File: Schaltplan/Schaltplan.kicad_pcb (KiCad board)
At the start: 2 copper layers, 12 parts, among them IC1 STM32G031J6M6, J1 Conn_01x01, J2 Conn_02x03_Odd_Even, SW1 SW_SPDT, U1 HU2032-LF

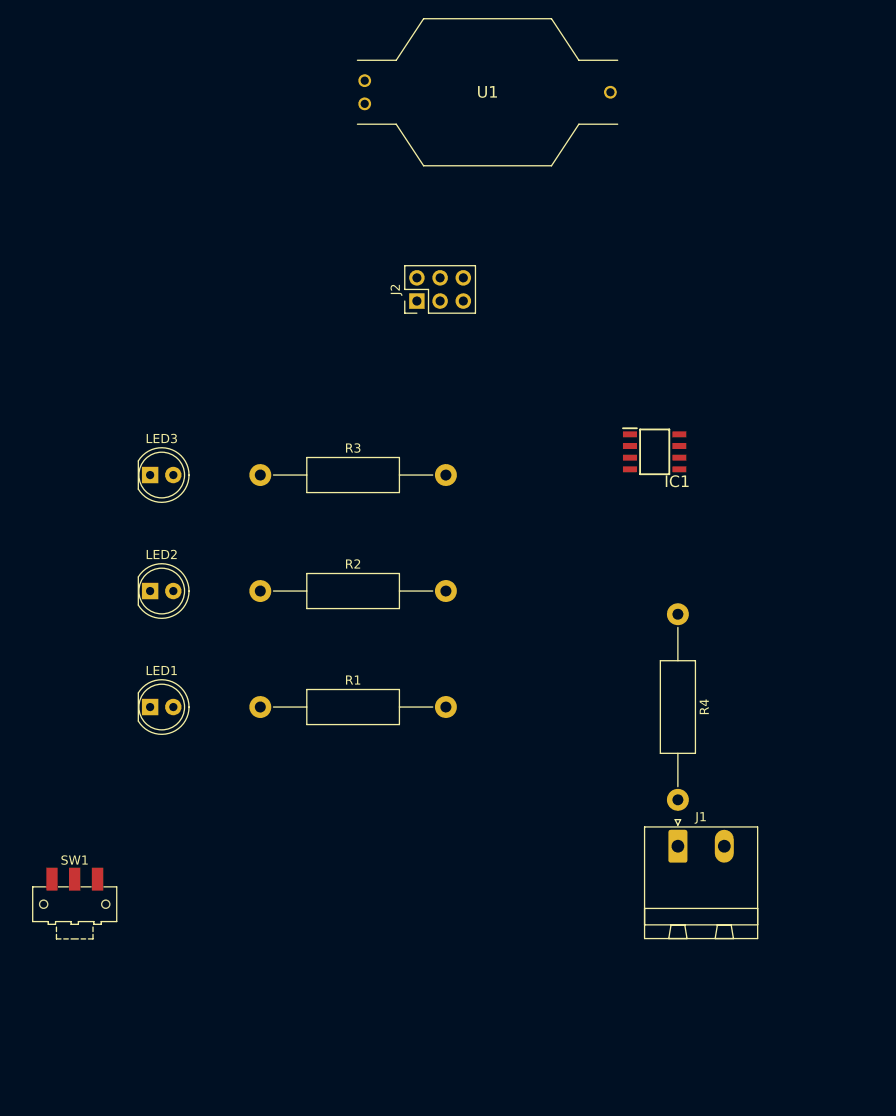
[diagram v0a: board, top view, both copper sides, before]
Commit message: ersten Leiterbahnen gezogen
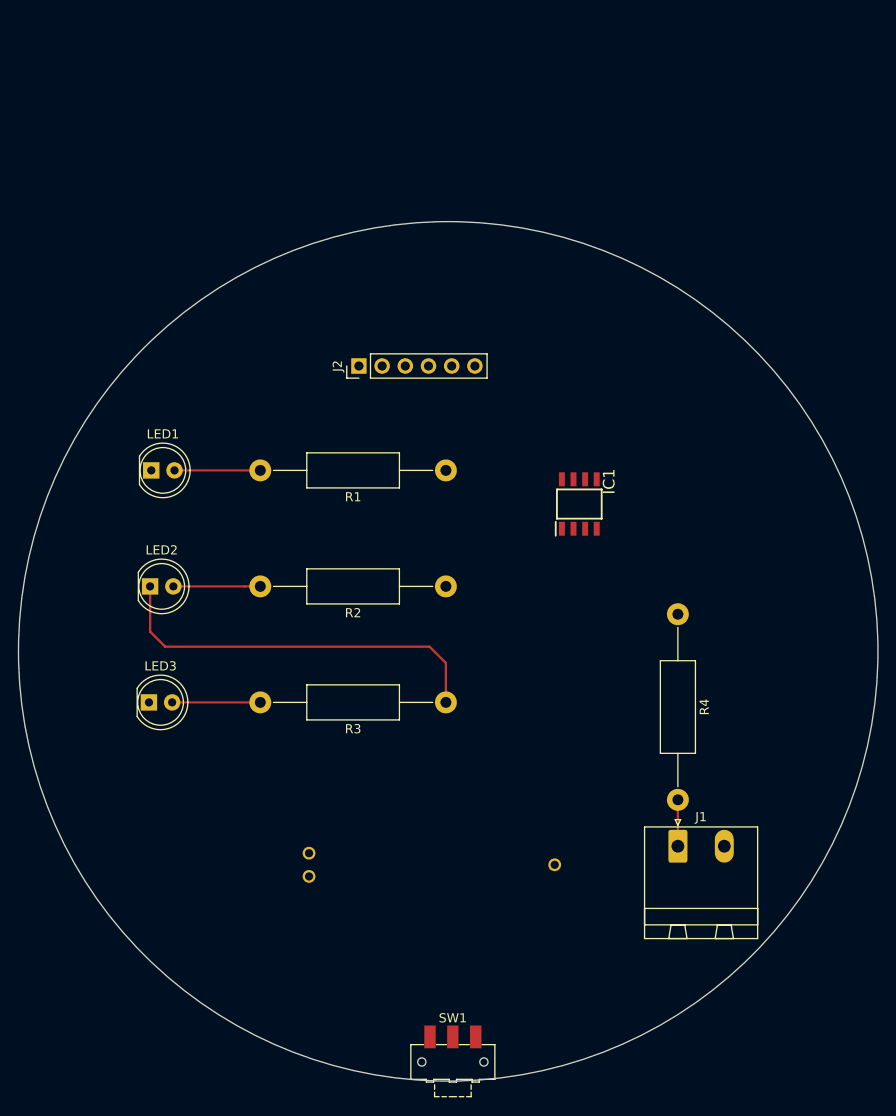
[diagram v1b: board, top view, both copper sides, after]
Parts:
- J2: value Conn_02x03_Odd_Even -> Conn_01x06_Male; footprint Connector_PinHeader_2.54mm:PinHeader_2x03_P2.54mm_Vertical -> Connector_PinHeader_2.54mm:PinHeader_1x06_P2.54mm_Vertical
- LED1: renamed from LED2; value yellow -> red
- LED2: renamed from LED1; value green -> yellow
- LED3: value red -> green
- R1: renamed from R2; value 82 Ohm -> 68 Ohm
- R2: renamed from R1; value 68 Ohm -> 82 Ohm
- U1: moved to B.Cu
- moved U1 87.3 mm to (127.3, 132.8)
- moved SW1 44.9 mm to (143.0, 153.2)
- moved R3 32.1 mm to (142.2, 113.8), turned to 180 degrees
- moved LED3 24.9 mm to (109.7, 113.8)
- moved R1 24.2 mm to (142.2, 88.4), turned to 180 degrees
- moved R2 24.2 mm to (142.2, 101.1), turned to 180 degrees
- moved LED1 13.2 mm to (110.0, 88.4)
- moved LED2 13.2 mm to (109.9, 101.1)
- moved IC1 10.0 mm to (156.8, 92.1), turned to 90 degrees
- moved J2 9.53 mm to (132.7, 77.0)
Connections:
- J2 pad 3: GND -> +3V3
- J2 pad 4: +3V3 -> GND
- SW1 pad 3: GND -> Net-(SW1-Pad3)
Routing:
- net PA8-LEDs: track 0.00 -> 43.1 mm
- net Net-(LED3-Pad2): track 0.00 -> 9.65 mm
- net Net-(LED2-Pad2): track 0.00 -> 9.53 mm
- net Net-(LED1-Pad2): track 0.00 -> 9.40 mm
- net PA12ReceivePin-kS: track 0.00 -> 5.08 mm
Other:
- board outline added: 94.1 x 94.1 mm
- net class Default: clearance 0.2 -> 0.25; via_dia 0.8 -> 0.6
- rule trace_clearance: 0.2 -> 0.25
- rule trace_min: 0.2 -> 0.25

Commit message: Leiterbahnen gezeichnet
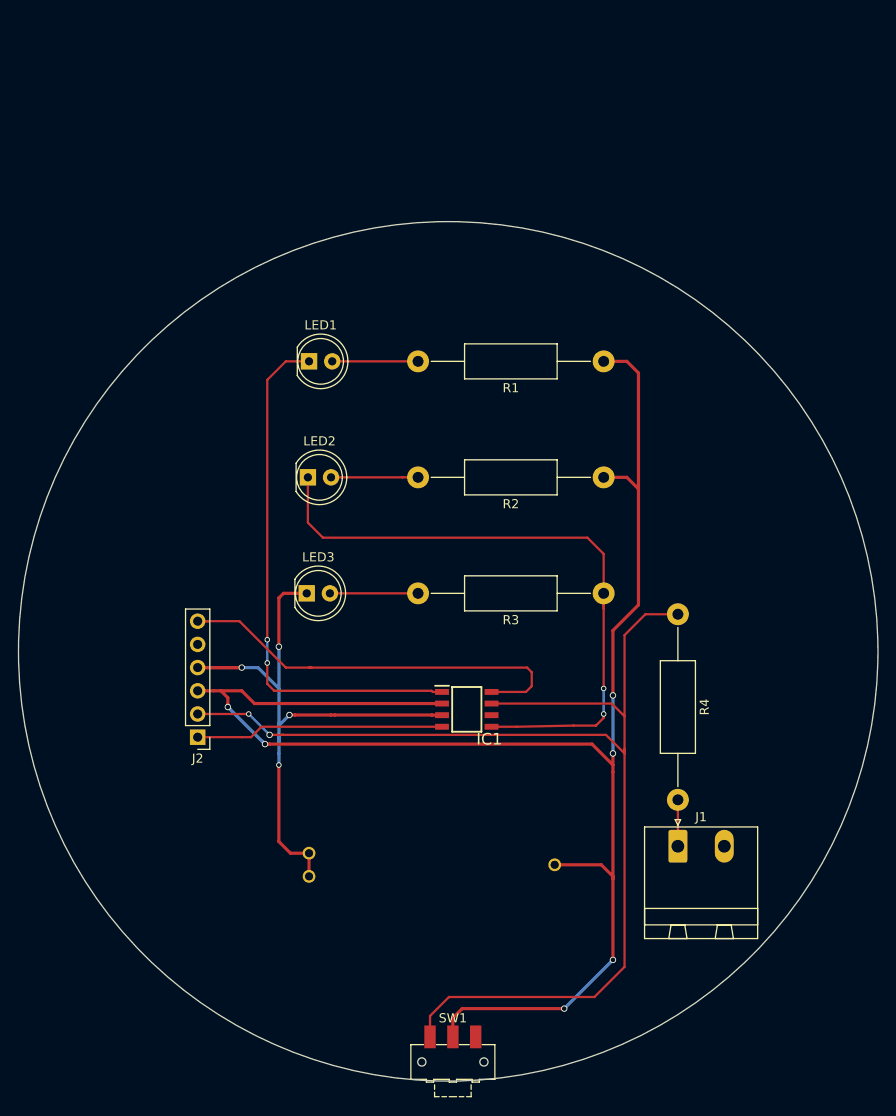
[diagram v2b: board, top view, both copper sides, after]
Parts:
- moved J2 44.3 mm to (115.1, 117.6), turned to 180 degrees
- moved IC1 25.6 mm to (144.5, 114.6), turned to 0 degrees
- moved LED1 21.0 mm to (127.3, 76.5)
- moved LED3 21.0 mm to (127.0, 101.9)
- moved LED2 21.0 mm to (127.1, 89.2)
- moved R1 21.0 mm to (159.5, 76.5)
- moved R2 21.0 mm to (159.5, 89.2)
- moved R3 21.0 mm to (159.5, 101.9)
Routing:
- net +3V3: track 0.00 -> 177.7 mm, vias 0 -> 6
- net Conn-SWDIO: track 0.00 -> 133.1 mm, vias 0 -> 2
- net GND: track 0.00 -> 70.1 mm, vias 0 -> 4
- net PB7-LEDs: track 0.00 -> 58.3 mm, vias 0 -> 2
- net Conn-SWCLK: track 0.00 -> 46.5 mm
- net PA8-LEDs: track 43.1 -> 71.0 mm, vias 0 -> 2
- net Conn-RST: track 0.00 -> 27.2 mm
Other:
- net class Power added: clearance 0.35, trace_width 0.35, via_dia 0.7, via_drill 0.5

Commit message: Schaltplan fertig Mi. 1.7.
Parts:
- added H1: MountingHole, MountingHole:MountingHole_4.5mm, F.Cu at (121.3, 71.7)
- added H2: MountingHole, MountingHole:MountingHole_4.5mm, F.Cu at (184.7, 108.6)
- added H3: MountingHole, MountingHole:MountingHole_4.5mm, F.Cu at (121.6, 144.9)
- J1: footprint Connector_Phoenix_MSTB:PhoenixContact_MSTBA_2,5_2-G-5,08_1x02_P5.08mm_Horizontal -> Connector_PinHeader_2.54mm:PinHeader_1x01_P2.54mm_Vertical
- moved J1 7.79 mm to (167.6, 137.3)
- moved LED1 1.67 mm to (127.0, 78.1)
- moved R1 1.65 mm to (159.5, 78.1)
- moved U1 1.04 mm to (127.3, 131.8)
- moved R3 0.90 mm to (159.4, 101.0)
- moved LED3 0.89 mm to (127.0, 101.0)
- moved LED2 0.40 mm to (127.0, 89.5)
- moved SW1 0.38 mm to (143.1, 152.8)
- moved R2 0.38 mm to (159.5, 89.5)
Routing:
- net PA12ReceivePin-kS: track 5.08 -> 13.4 mm
- net +3V3: track 177.7 -> 175.8 mm
- net PB7-LEDs: track 58.3 -> 56.5 mm
- added copper zone on B.Cu, net GND
- added copper zone on F.Cu, net GND
